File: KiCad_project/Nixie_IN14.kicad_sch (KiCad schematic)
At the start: 65 parts, among them J1 Conn_01x10_Pin, J2 Conn_01x07_Pin, J3 Conn_01x07_Pin, J4 Conn_01x10_Pin, J5 Conn_01x07_Pin, J6 Conn_01x07_Pin, J7 USB_C_Receptacle_PowerOnly_6P, Q1 IRF540N, Q2 MMBTA42, U1 BME280_module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

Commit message: fixed connection error replaced and rerouted
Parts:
- BZ1: footprint Buzzer_Beeper:Buzzer_D14mm_H7mm_P10mm -> Buzzer_Beeper:Buzzer_TDK_PS1240P02BT_D12.2mm_H6.5mm
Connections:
- net A1: now also J6.3 (Pin_3); no longer J5.3 (Pin_3)
- net A2: now also J6.4 (Pin_4); no longer J5.4 (Pin_4)
- net A3: now also J6.5 (Pin_5); no longer J5.5 (Pin_5)
- net A4: now also J6.6 (Pin_6); no longer J5.6 (Pin_6)
- net A5: now also J5.6 (Pin_6); no longer J6.6 (Pin_6)
- net A6: now also J5.7 (Pin_7); no longer J6.7 (Pin_7)
- net LED_B: now also J5.3 (Pin_3); no longer J6.4 (Pin_4)
- net LED_B_NCC: now also J6.7 (Pin_7); no longer J5.7 (Pin_7)
- net LED_B_top: now also J3.3 (Pin_3); no longer J3.4 (Pin_4)
- net LED_G: now also J5.2 (Pin_2); no longer J6.3 (Pin_3)
- net LED_G_top: now also J3.2 (Pin_2); no longer J3.3 (Pin_3)
- net LED_R: now also J5.4 (Pin_4); no longer J6.2 (Pin_2)
- net LED_R_top: now also J3.4 (Pin_4); no longer J3.2 (Pin_2)
- net SEC_1: now also J6.2 (Pin_2); no longer J5.2 (Pin_2)
- net SEC_2: now also J5.5 (Pin_5); no longer J6.5 (Pin_5)
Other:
- moved on the sheet: J5, J6

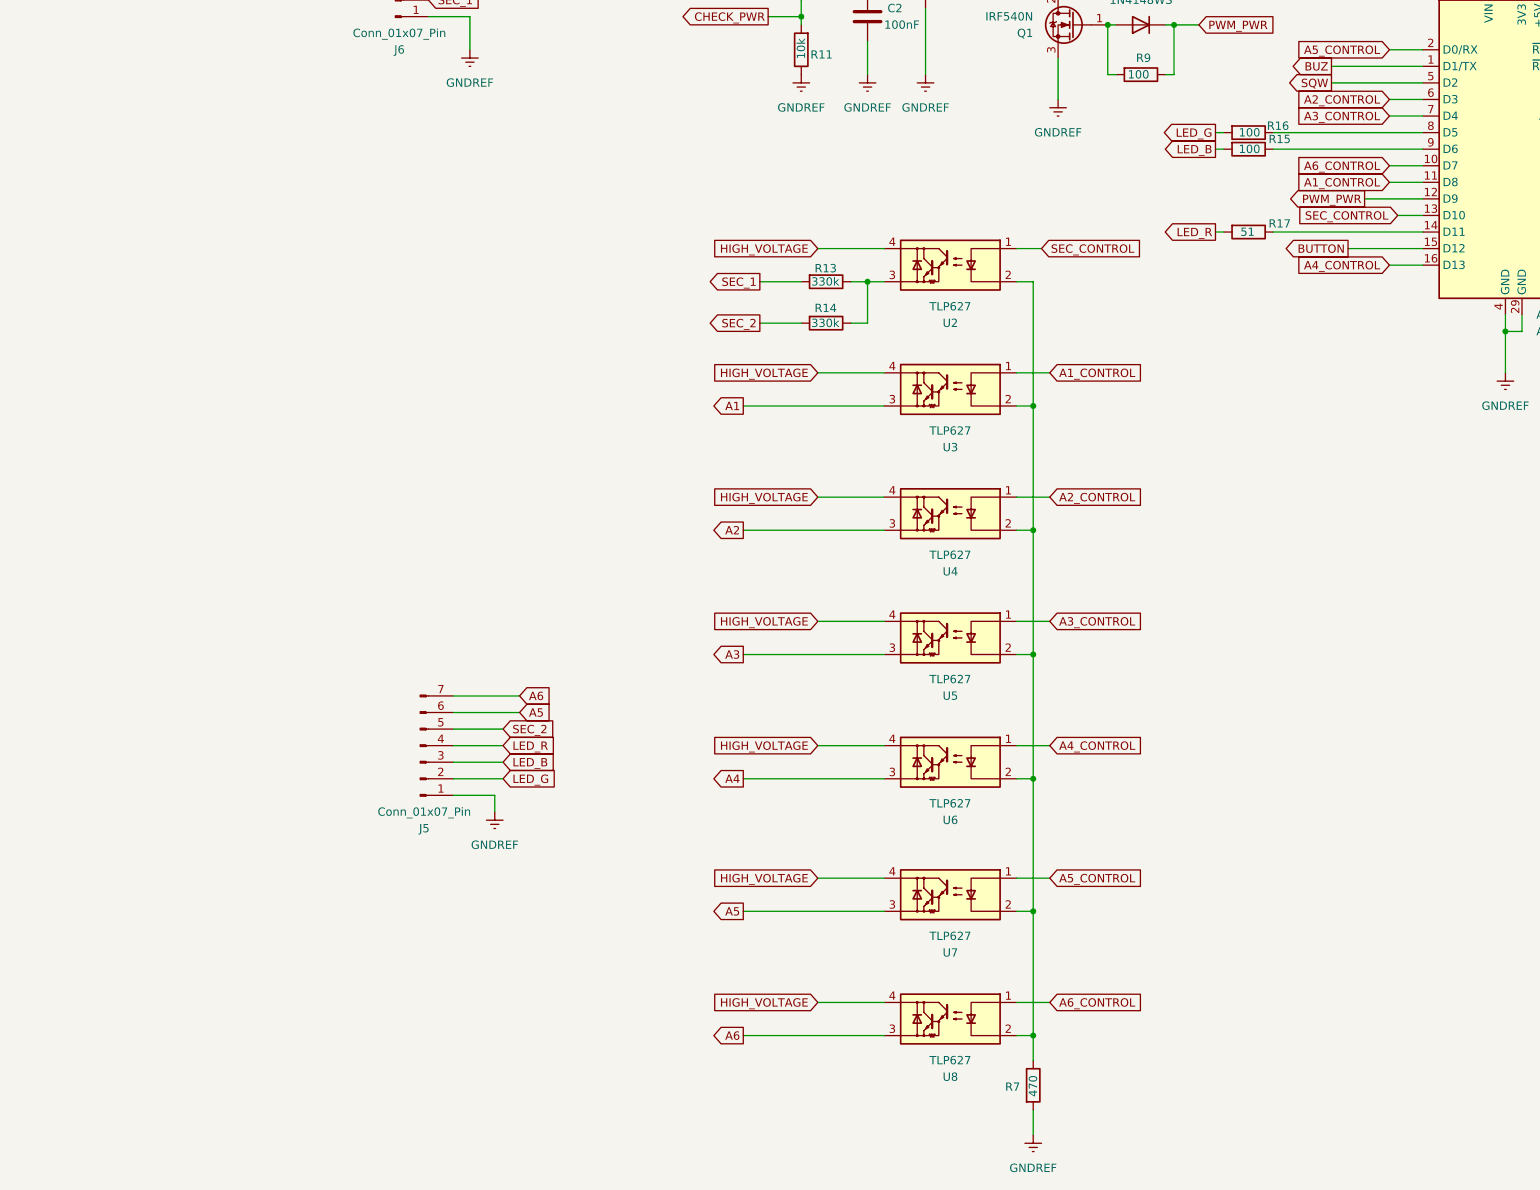
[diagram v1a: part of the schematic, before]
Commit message: added power keys for LEDs resistor pacjakges changed from 0805 to 1206
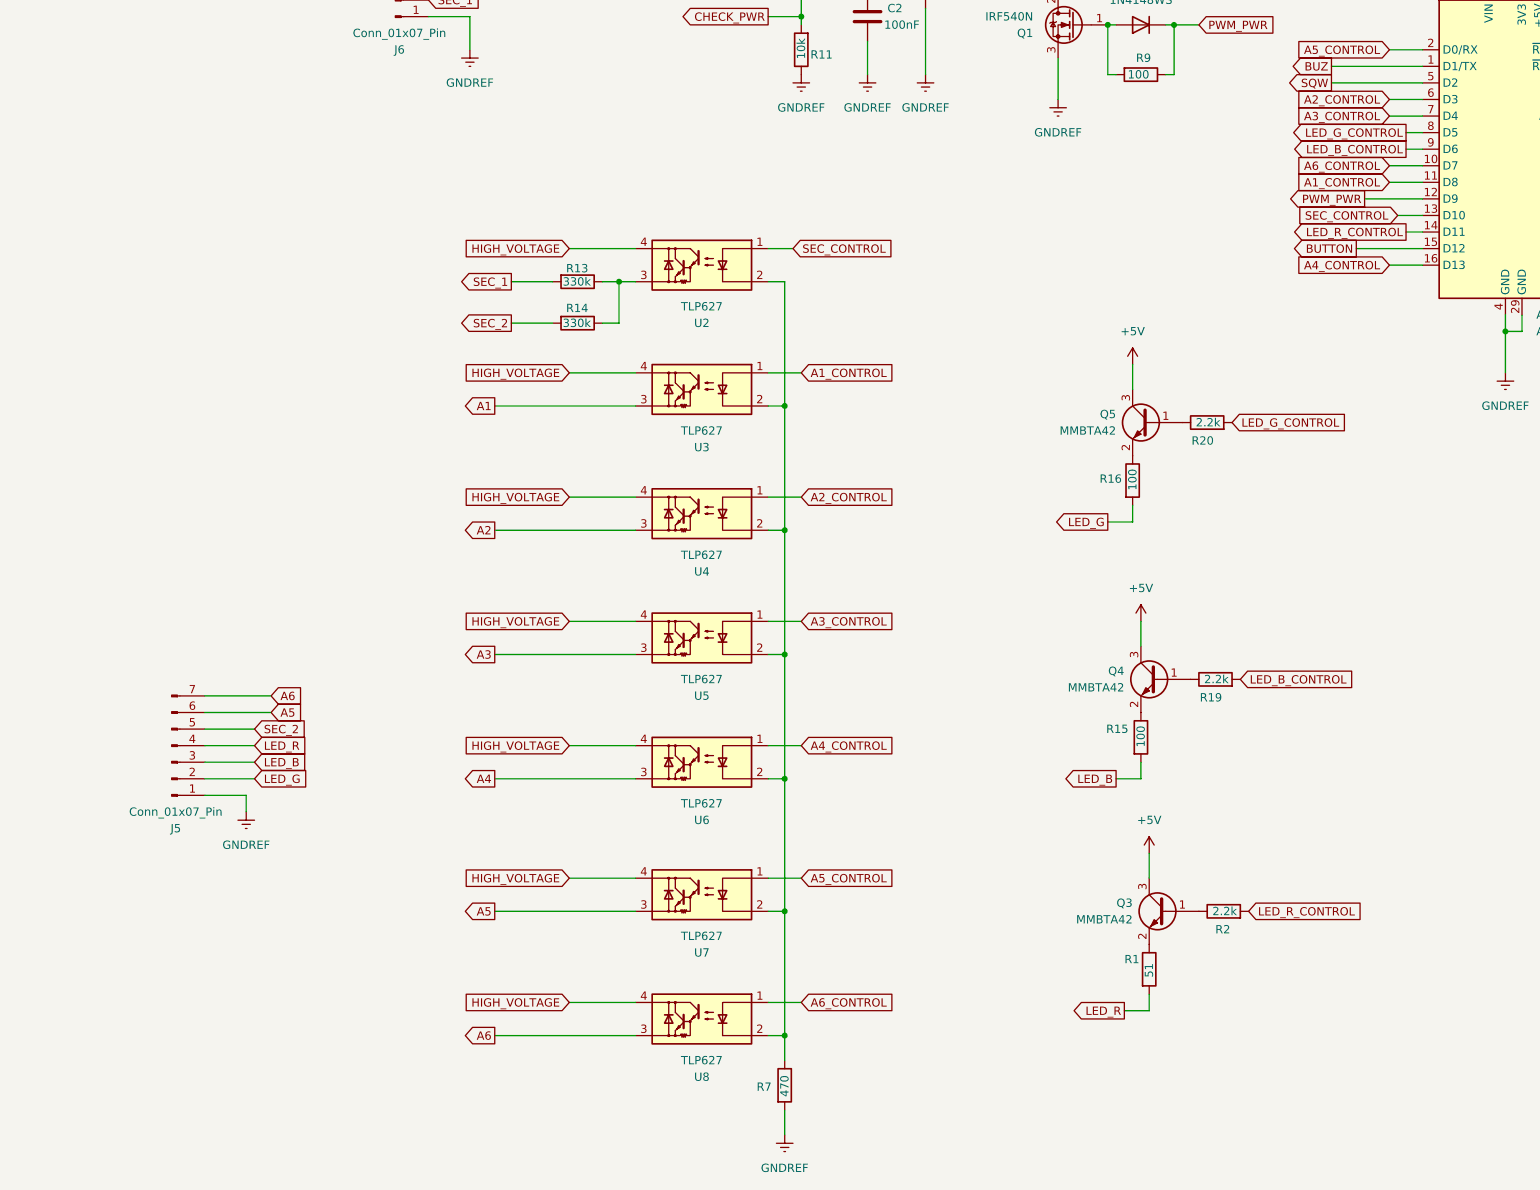
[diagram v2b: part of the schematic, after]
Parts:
- removed R17: 51, Resistor_SMD:R_0805_2012Metric_Pad1.20x1.40mm_HandSolder, symbol Device:R
- added Q3, Q4, Q5: MMBTA42, Package_TO_SOT_SMD:SOT-23, symbol Transistor_BJT:MMBTA42
- added R1: 51, Resistor_SMD:R_1206_3216Metric_Pad1.30x1.75mm_HandSolder, symbol Device:R
- added R19, R2, R20: 2.2k, Resistor_SMD:R_1206_3216Metric_Pad1.30x1.75mm_HandSolder, symbol Device:R
- R10, R11, R12, R13, R14, R15, R16, R18, R3, R4, R5, R6, R7, R8, R9: footprint Resistor_SMD:R_0805_2012Metric_Pad1.20x1.40mm_HandSolder -> Resistor_SMD:R_1206_3216Metric_Pad1.30x1.75mm_HandSolder
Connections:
- net +5V: now also Q3.3 (C), Q4.3 (C), Q5.3 (C)
- net LED_R: now also R1.2
- net LED_R_CONTROL: now reaches A1.14 (D11)
- net LED_R_CONTROL: now also R2.2
- net at R16.1: now also Q5.2 (E); no longer A1.8 (D5)
- net at R15.1: now also Q4.2 (E); no longer A1.9 (D6)
- new net: Q3.1 (B), R2.1
- new net: Q3.2 (E), R1.1
- new net: Q5.1 (B), R20.1
- new net: Q4.1 (B), R19.1
- new net LED_B_CONTROL: A1.9 (D6), R19.2
- new net LED_G_CONTROL: A1.8 (D5), R20.2
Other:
- moved on the sheet: J5, R13, R14, R7, U2, U3, U4, U5, U6, U7, U8
